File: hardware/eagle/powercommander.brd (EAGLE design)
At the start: 100 x 85 mm, 28 parts, among them IC1 ULN2803SO18-1, IC2 7805TV, IC3 MCP2551DIL8, K1 G5NB, K2 G5NB, K3 G5NB, K4 G5NB, K5 G5NB, K6 G5NB, K7 G5NB, K8 G5NB, X2 3KLEMME, X3 2KLEMME, X4 2KLEMME, X5 2KLEMME, X6 2KLEMME

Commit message: neu verkabelt
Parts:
- removed EXT2: EXT2, pinhead:2X13
- added D1, D2, D3, D4, D5, D6, D7, D8: (no value), diode:SOD323-W
- added D9: (no value), diode:MELF-MLL41
- added EXT2-1-4, EXT2-23-26: (no value), pinhead:2X02
- added F2: FUSESH35, fuse:SH25
- IC3: value MCP2551DIL8 -> MCP2551SOIC8; device personal-parts:DIL8 -> personal-parts:SOIC-08LG
- moved K1 16.3 mm to (57.1, 24.1)
- moved C3 11.4 mm to (58.4, 77.5)
- moved K3 5.24 mm to (41.9, 24.1)
- moved K7 5.24 mm to (11.4, 24.1)
- moved K8 5.24 mm to (3.81, 24.1)
- moved K2 5.24 mm to (49.5, 24.1)
- moved K4 5.24 mm to (34.3, 24.1)
- moved K5 5.24 mm to (26.7, 24.1)
- moved K6 5.24 mm to (19.1, 24.1)
- moved X5 5.08 mm to (24.2, 4.50)
- moved X6 5.08 mm to (14.1, 4.50)
- moved X3 5.08 mm to (44.6, 4.50)
- moved X4 5.08 mm to (34.4, 4.50)
- moved IC3 2.54 mm to (14.0, 59.7), flipped to the bottom, turned to 270 degrees
- moved C2 1.80 mm to (49.5, 76.2)
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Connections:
- net A2 renamed N$14
- net A4 renamed N$9
- net A6 renamed N$12
- net A8 renamed N$13
- removed net N$12 (its old number): IC1.14, K4.1
- removed net N$13 (its old number): IC1.15, K5.1
- removed net N$14 (its old number): IC1.16, K6.1
- removed net N$16: IC1.18, K8.1
- removed net N$21: EXT1.7, IC1.1
- removed net N$9 (its old number): IC1.11, K1.1
- new net N$22: F2.1, PHASE.2
- new net N$24: D8.A, IC1.18, K8.4
- new net N$26: D6.A, IC1.16, K6.4
- new net N$27: D5.A, IC1.15, K5.4
- new net N$28: D4.A, IC1.14, K4.4
- net +5V: now also D1.C, D2.C, D3.C, D4.C, D5.C, D6.C, D7.C, D8.C, D9.A, EXT2-23-26.4, K1.1, K2.1, K3.1, K4.1, K5.1, K6.1, K7.1, K8.1; no longer EXT2.26, K1.4, K2.4, K3.4, K4.4, K5.4, K6.4, K7.4, K8.4
- net N$10: now also D2.A, K2.4; no longer K2.1
- net N$11: now also D3.A, K3.4; no longer K3.1
- net N$15: now also D7.A, K7.4; no longer K7.1
- net N$2: now also X2.2; no longer X2.1
- net N$20: now also D1.A, IC1.11, K1.4; no longer EXT1.9, IC1.2
- net N$5: now also D9.C
- net N$6: now also X2.1; no longer X2.2
- net NULL: now also PHASE.1; no longer PHASE.2
- net PHASE: now also F2.2; no longer PHASE.1
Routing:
- net N$9 (its old number): track 49.9 -> 0.00 mm
- net N$16: track 32.3 -> 0.00 mm
- net N$24: track 0.00 -> 31.7 mm
- net N$20: track 9.13 -> 36.3 mm
- net N$35: track 25.7 -> 4.58 mm
- net N$14 (its old number): track 20.4 -> 0.00 mm
- net PHASE: track 134.3 -> 114.1 mm
- net N$12 (its old number): track 19.6 -> 0.00 mm
- net N$26: track 0.00 -> 19.1 mm
- net N$28: track 0.00 -> 17.5 mm
- net N$13 (its old number): track 17.0 -> 0.00 mm
- net N$27: track 0.00 -> 16.2 mm
- net N$22: track 0.00 -> 13.7 mm
- net N$21: track 10.5 -> 0.00 mm
- net N$19: track 8.60 -> 0.00 mm
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
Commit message: neue board version mit pwm pins
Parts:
- removed EXT2-23-26: (no value), pinhead:2X02
- added EXT2-21-26: (no value), pinhead:2X03
- moved JP3 34.4 mm to (6.30, 78.1), turned to 0 degrees
- moved IC3 32.3 mm to (46.2, 58.8), turned to 180 degrees
- moved R1 32.0 mm to (2.49, 70.5), turned to 270 degrees
- moved R2 28.8 mm to (5.03, 70.5), turned to 270 degrees
- moved R3 25.8 mm to (7.57, 70.5), turned to 270 degrees
- moved X2 9.00 mm to (21.6, 80.5)
- moved IC1 6.25 mm to (25.0, 53.8)
- flipped EXT1 to the bottom
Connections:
- removed net N$18 (its old number): EXT1.13, IC1.4
- removed net N$38: EXT1.16, R3.2
- removed net N$39: EXT1.14, R2.2
- removed net N$40: EXT1.12, R1.2
- new net N$16: EXT1.17, IC1.4
- new net N$21: EXT1.13, IC1.7
- new net N$25: EXT1.14, IC1.8
- new net N$29: EXT1.24, R1.2
- new net N$31: EXT1.18, R3.2
- net +5V: now also EXT2-21-26.6; no longer EXT2-23-26.4
- net N$1: now also EXT1.26, IC1.1; no longer EXT1.21, IC1.8
- net N$19: now also EXT1.16, IC1.6; no longer EXT1.11, IC1.3
- net N$30: now also EXT1.20, R2.2; no longer EXT1.26, IC1.10
- net N$7: now also EXT1.22, IC1.2; no longer EXT1.19, IC1.7
- net N$8: now also EXT1.21, IC1.3; no longer EXT1.17, IC1.6
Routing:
- net N$31: track 0.00 -> 25.8 mm
- net +5V: track 232.0 -> 209.4 mm
- net N$29: track 0.00 -> 21.2 mm
- net N$40: track 16.6 -> 0.00 mm
- net N$6: track 30.3 -> 45.0 mm
- net N$1: track 0.00 -> 12.1 mm
- net GND: track 12.1 -> 0.00 mm
- net N$39: track 11.9 -> 0.00 mm
- net N$7: track 0.00 -> 11.7 mm
- net N$2: track 28.8 -> 39.9 mm
- net N$25: track 0.00 -> 10.4 mm
- net N$19: track 0.00 -> 10.4 mm
- net N$8: track 0.00 -> 8.56 mm
- net N$30: track 32.0 -> 23.9 mm
- net N$38: track 7.77 -> 0.00 mm
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
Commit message: some fixes..
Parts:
- moved R3 8.10 mm to (13.9, 75.6), turned to 0 degrees
- moved R2 6.84 mm to (11.4, 73.1), turned to 0 degrees
- moved R1 6.27 mm to (8.76, 70.6), turned to 0 degrees
- moved X2 5.00 mm to (26.6, 80.5)
- moved JP3 3.05 mm to (8.78, 79.9)
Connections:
- net GND: now also EXT2-21-26.5
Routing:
- net N$29: track 21.2 -> 4.43 mm
- net N$30: track 23.9 -> 8.50 mm
- net N$31: track 25.8 -> 10.8 mm
- net N$32: track 3.81 -> 9.27 mm
- net N$36: track 3.81 -> 6.86 mm
- net N$6: track 45.0 -> 42.0 mm
- net N$2: track 39.9 -> 37.1 mm
- net N$37: track 3.81 -> 4.32 mm
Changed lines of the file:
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@@
 <element name="IC1" library="personal-parts" package="SO18-1" value="ULN2803SO18-1" x="25" y="53.75" rot="MR180"/>
 <element name="PHASE" library="personal-parts" package="W237-102" value="2KLEMME" x="91" y="4.5"/>
-<element name="X2" library="personal-parts" package="W237-103" value="3KLEMME" x="21.62" y="80.5" rot="R180"/>
+<element name="X2" library="personal-parts" package="W237-103" value="3KLEMME" x="26.62" y="80.5" rot="R180"/>
 <element name="IC2" library="linear" package="TO220V" value="7805TV" x="64.77" y="76.2" rot="R270"/>
 <element name="B1" library="rectifier" package="RB1A" value="rectifier" x="87.63" y="76.2"/>
@@
 <element name="X6" library="personal-parts" package="W237-102" value="2KLEMME" x="14.08" y="4.5"/>
 <element name="IC3" library="personal-parts" package="SOIC-08LG" value="MCP2551SOIC8" x="46.25" y="58.75" rot="MR180"/>
-<element name="JP3" library="pinhead" package="1X04" value="LEDS" x="6.3" y="78.14"/>
-<element name="R1" library="rcl" package="0204/7" value="280R" x="2.49" y="70.52" rot="R270"/>
-<element name="R2" library="rcl" package="0204/7" value="280R" x="5.03" y="70.52" rot="R270"/>
-<element name="R3" library="rcl" package="0204/7" value="280R" x="7.57" y="70.52" rot="R270"/>
+<element name="JP3" library="pinhead" package="1X04" value="LEDS" x="8.78" y="79.918"/>
+<element name="R1" library="rcl" package="0204/7" value="280R" x="8.758" y="70.645"/>
+<element name="R2" library="rcl" package="0204/7" value="280R" x="11.385" y="73.058"/>
+<element name="R3" library="rcl" package="0204/7" value="280R" x="13.885" y="75.598"/>
 <element name="F2" library="fuse" package="SH25" value="FUSESH35" x="85.09" y="16.51" rot="R180">
 <attribute name="OC_NEWARK" value="unknown" x="85.09" y="16.51" size="1.778" layer="27" rot="R180" display="off"/>
@@
 </polygon>
 <contactref element="EXT1" pad="6"/>
-<wire x1="38.735" y1="67.945" x2="45.615" y2="61.425" width="0" layer="19" extent="16-16"/>
+<contactref element="EXT2-21-26" pad="5"/>
 </signal>
 <signal name="A1">
@@
 <contactref element="JP3" pad="1"/>
 <contactref element="R1" pad="1"/>
-<wire x1="2.49" y1="78.14" x2="2.49" y2="74.33" width="1.27" layer="16"/>
+<wire x1="4.97" y1="79.918" x2="4.948" y2="70.645" width="1.27" layer="16"/>
 </signal>
 <signal name="N$36">
 <contactref element="JP3" pad="2"/>
 <contactref element="R2" pad="1"/>
-<wire x1="5.03" y1="78.14" x2="5.03" y2="74.33" width="1.27" layer="16"/>
+<wire x1="7.51" y1="79.918" x2="7.575" y2="73.058" width="1.27" layer="16"/>
 </signal>
 <signal name="N$37">
 <contactref element="JP3" pad="3"/>
 <contactref element="R3" pad="1"/>
-<wire x1="7.57" y1="78.14" x2="7.57" y2="74.33" width="1.27" layer="16"/>
+<wire x1="10.05" y1="79.918" x2="10.075" y2="75.598" width="1.27" layer="16"/>
 </signal>
 <signal name="N$11">
@@
 <wire x1="40" y1="53.75" x2="35" y2="58.75" width="0.4064" layer="16"/>
 <wire x1="35" y1="58.75" x2="35" y2="72.14" width="0.4064" layer="16"/>
-<wire x1="35" y1="72.14" x2="26.62" y2="80.52" width="0.4064" layer="16"/>
+<wire x1="35" y1="72.14" x2="31.62" y2="80.52" width="0.4064" layer="16"/>
 </signal>
 <signal name="N$6">
@@
 <wire x1="40" y1="52.5" x2="32.5" y2="60" width="0.4064" layer="16"/>
 <wire x1="32.5" y1="60" x2="32.5" y2="69.64" width="0.4064" layer="16"/>
-<wire x1="32.5" y1="69.64" x2="21.62" y2="80.52" width="0.4064" layer="16"/>
+<wire x1="32.5" y1="69.64" x2="26.62" y2="80.52" width="0.4064" layer="16"/>
 </signal>
 <signal name="N$29">
 <contactref element="EXT1" pad="24"/>
 <contactref element="R1" pad="2"/>
-<wire x1="15.875" y1="67.945" x2="15.875" y2="69.469" width="0.4064" layer="16"/>
-<wire x1="15.875" y1="69.469" x2="15.113" y2="70.231" width="0.4064" layer="16"/>
-<wire x1="15.113" y1="70.231" x2="10.668" y2="70.231" width="0.4064" layer="16"/>
-<wire x1="10.668" y1="70.231" x2="10.668" y2="66.421" width="0.4064" layer="16"/>
-<wire x1="10.668" y1="66.421" x2="8.255" y2="64.008" width="0.4064" layer="16"/>
-<wire x1="8.255" y1="64.008" x2="5.192" y2="64.008" width="0.4064" layer="16"/>
-<wire x1="5.192" y1="64.008" x2="2.49" y2="66.71" width="0.4064" layer="16"/>
+<wire x1="15.875" y1="67.945" x2="13.175" y2="70.645" width="1.27" layer="16" curve="90"/>
+<wire x1="13.175" y1="70.645" x2="12.568" y2="70.645" width="1.27" layer="16"/>
 </signal>
 <signal name="N$30">
 <contactref element="EXT1" pad="20"/>
 <contactref element="R2" pad="2"/>
-<wire x1="20.955" y1="67.945" x2="20.955" y2="69.088" width="0.4064" layer="16"/>
-<wire x1="20.955" y1="69.088" x2="18.542" y2="71.501" width="0.4064" layer="16"/>
-<wire x1="18.542" y1="71.501" x2="9.779" y2="71.501" width="0.4064" layer="16"/>
-<wire x1="9.779" y1="71.501" x2="9.652" y2="71.374" width="0.4064" layer="16"/>
-<wire x1="9.652" y1="71.374" x2="9.652" y2="67.056" width="0.4064" layer="16"/>
-<wire x1="9.652" y1="67.056" x2="7.747" y2="65.151" width="0.4064" layer="16"/>
-<wire x1="7.747" y1="65.151" x2="6.589" y2="65.151" width="0.4064" layer="16"/>
-<wire x1="6.589" y1="65.151" x2="5.03" y2="66.71" width="0.4064" layer="16"/>
+<wire x1="20.955" y1="67.945" x2="20.955" y2="69.85" width="1.27" layer="16"/>
+<wire x1="20.955" y1="69.85" x2="15.195" y2="73.058" width="1.27" layer="16"/>
 </signal>
 <signal name="N$31">
 <contactref element="EXT1" pad="18"/>
 <contactref element="R3" pad="2"/>
-<wire x1="7.57" y1="66.71" x2="7.57" y2="71.18" width="0.4064" layer="16"/>
-<wire x1="7.57" y1="71.18" x2="7.5" y2="72.52" width="0.4064" layer="16"/>
-<wire x1="7.5" y1="72.52" x2="22.5" y2="72.52" width="0.4064" layer="16"/>
-<wire x1="22.5" y1="72.52" x2="23.75" y2="70" width="0.4064" layer="16"/>
-<wire x1="23.75" y1="70" x2="23.75" y2="68.2" width="0.4064" layer="16"/>
-<wire x1="23.75" y1="68.2" x2="23.495" y2="67.945" width="0.4064" layer="16"/>
+<wire x1="23.495" y1="67.945" x2="23.495" y2="70.993" width="1.27" layer="16"/>
+<wire x1="23.495" y1="70.993" x2="18.89" y2="75.598" width="1.27" layer="16"/>
+<wire x1="18.89" y1="75.598" x2="17.695" y2="75.598" width="1.27" layer="16"/>
 </signal>
 </signals>

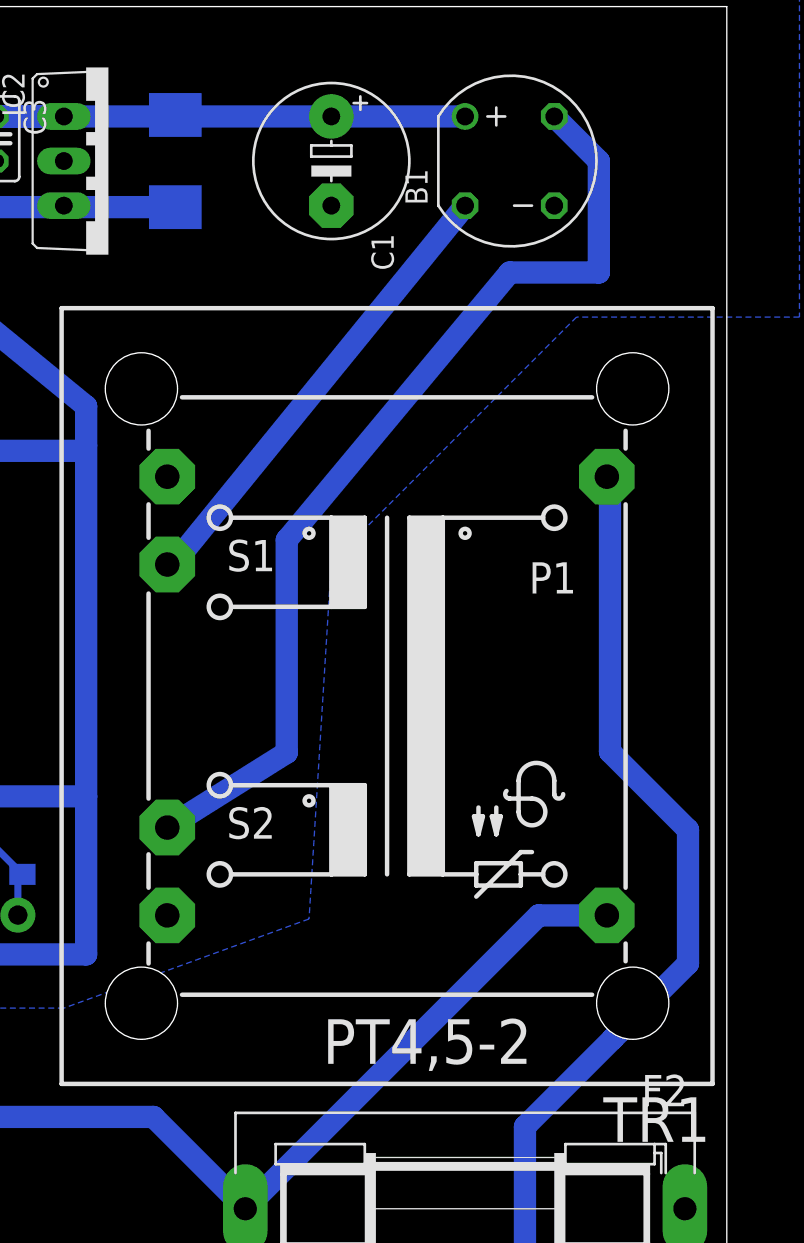
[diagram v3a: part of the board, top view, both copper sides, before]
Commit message: removed transformer holes
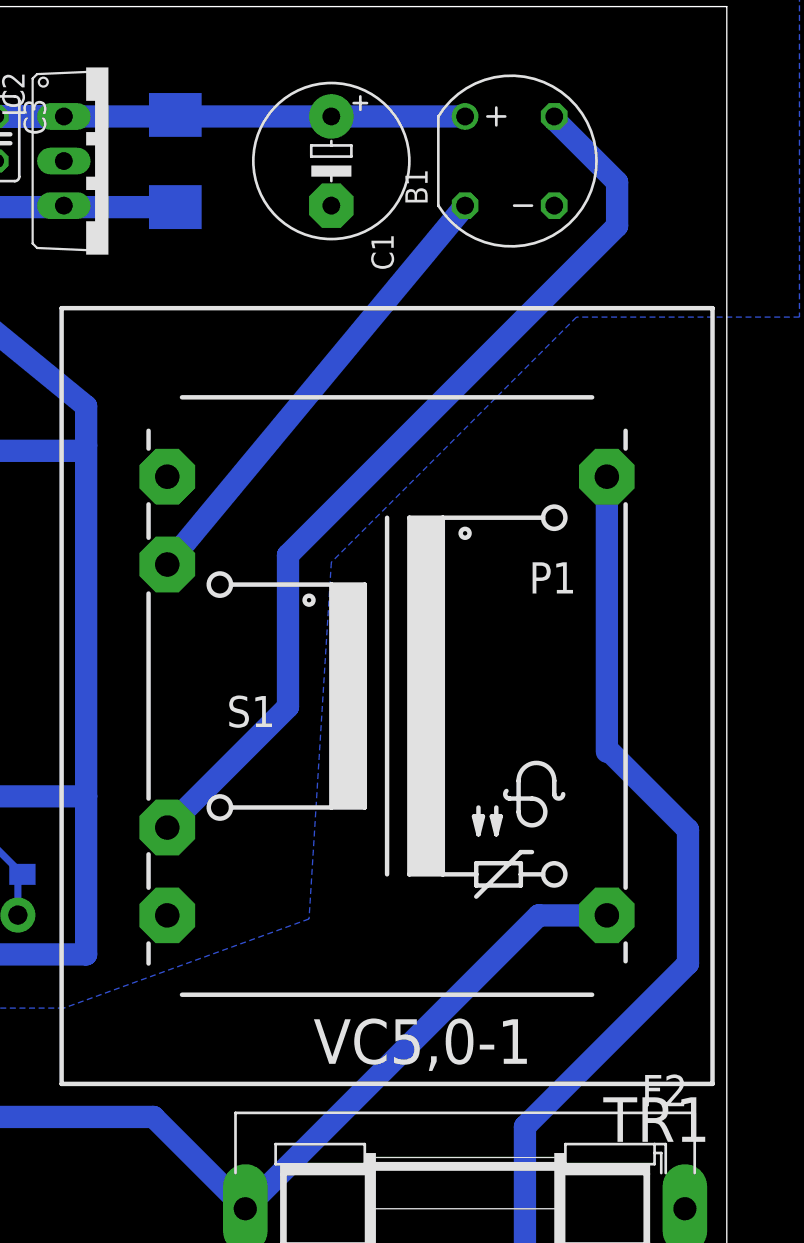
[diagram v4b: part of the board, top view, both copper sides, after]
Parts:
- TR1: value TRAFO 9V 556mA -> (none); device trafo:PT04,5-2 -> personal-parts:VC5,0-1
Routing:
- net N$4: track 55.0 -> 52.6 mm
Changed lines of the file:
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@@
 <element name="IC2" library="linear" package="TO220V" value="7805TV" x="64.77" y="76.2" rot="R270"/>
 <element name="B1" library="rectifier" package="RB1A" value="rectifier" x="87.63" y="76.2"/>
-<element name="TR1" library="trafo" package="PT04,5-2" value="TRAFO 9V 556mA" x="80.645" y="45.72" rot="R180"/>
 <element name="K1" library="relay-omron-G5NB" package="G5NB" value="G5NB" x="57.15" y="24.13" rot="R270">
 <attribute name="OC_NEWARK" value="unknown" x="-33.02" y="0" size="1.778" layer="27" rot="R270" display="off"/>
@@
 <element name="EXT2-21-26" library="pinhead" package="2X03" value="" x="41.075" y="41.275" rot="MR180"/>
 <element name="EXT2-1-4" library="pinhead" package="2X02" value="" x="14.605" y="41.275" rot="R270"/>
+<element name="TR1" library="personal-parts" package="VC5,0-1" value="" x="80.645" y="45.72" rot="R180"/>
 </elements>
 <signals>
 <signal name="PHASE">
-<contactref element="TR1" pad="1"/>
 <contactref element="K8" pad="2"/>
 <contactref element="K7" pad="2"/>
@@
 <wire x1="72.5678" y1="16.51" x2="67.3378" y2="21.74" width="1.27" layer="16"/>
 <wire x1="67.3378" y1="21.74" x2="54.91" y2="21.74" width="1.27" layer="16"/>
+<wire x1="89.281" y1="33.2232" x2="72.5678" y2="16.51" width="1.27" layer="16"/>
+<contactref element="TR1" pad="1"/>
 <wire x1="93.1672" y1="33.2232" x2="89.281" y2="33.2232" width="1.27" layer="16"/>
-<wire x1="89.281" y1="33.2232" x2="72.5678" y2="16.51" width="1.27" layer="16"/>
 </signal>
 <signal name="NULL">
-<contactref element="TR1" pad="2"/>
-<wire x1="93.5" y1="26.19" x2="93.98" y2="26.67" width="1.27" layer="16"/>
-<wire x1="93.98" y1="26.67" x2="97.79" y2="30.48" width="1.27" layer="16"/>
 <wire x1="97.79" y1="30.48" x2="97.79" y2="38.1" width="1.27" layer="16"/>
 <wire x1="97.79" y1="38.1" x2="93.345" y2="42.545" width="1.27" layer="16"/>
-<wire x1="93.345" y1="42.545" x2="93.345" y2="58.039" width="1.27" layer="16"/>
-<wire x1="93.345" y1="58.039" x2="93.1672" y2="58.2168" width="0.4064" layer="16"/>
 <contactref element="PHASE" pad="1"/>
 <wire x1="88.5" y1="4.5" x2="88.5" y2="21.19" width="1.27" layer="16"/>
-<wire x1="88.5" y1="21.19" x2="93.5" y2="26.19" width="1.27" layer="16"/>
-</signal>
-<signal name="N$3">
-<contactref element="TR1" pad="5"/>
-<contactref element="B1" pad="AC1"/>
-<wire x1="68.1228" y1="38.227" x2="74.93" y2="42.4942" width="1.27" layer="16"/>
-<wire x1="74.93" y1="42.4942" x2="74.93" y2="54.61" width="1.27" layer="16"/>
-<wire x1="74.93" y1="54.61" x2="87.63" y2="69.85" width="1.27" layer="16"/>
-<wire x1="87.63" y1="69.85" x2="92.71" y2="69.85" width="1.27" layer="16"/>
-<wire x1="92.71" y1="69.85" x2="92.71" y2="76.2" width="1.27" layer="16"/>
-<wire x1="92.71" y1="76.2" x2="90.17" y2="78.74" width="1.27" layer="16"/>
-</signal>
-<signal name="N$4">
-<contactref element="TR1" pad="4"/>
-<contactref element="B1" pad="AC2"/>
-<wire x1="68.1228" y1="53.213" x2="68.453" y2="53.213" width="0.4064" layer="16"/>
-<wire x1="68.453" y1="53.213" x2="85.09" y2="73.66" width="1.27" layer="16"/>
+<wire x1="88.5" y1="21.19" x2="97.79" y2="30.48" width="1.27" layer="16"/>
+<contactref element="TR1" pad="2"/>
+<wire x1="93.345" y1="42.545" x2="93.1672" y2="42.545" width="0.4064" layer="16"/>
+<wire x1="93.1672" y1="42.545" x2="93.1672" y2="58.2168" width="1.27" layer="16"/>
 </signal>
 <signal name="N$5">
@@
 <wire x1="18.89" y1="75.598" x2="17.695" y2="75.598" width="1.27" layer="16"/>
 </signal>
+<signal name="N$3">
+<contactref element="TR1" pad="4"/>
+<contactref element="B1" pad="AC2"/>
+<wire x1="68.1228" y1="53.213" x2="85.09" y2="73.66" width="1.27" layer="16"/>
+</signal>
+<signal name="N$4">
+<contactref element="TR1" pad="5"/>
+<contactref element="B1" pad="AC1"/>
+<wire x1="68.1228" y1="38.227" x2="75" y2="45.1042" width="1.27" layer="16"/>
+<wire x1="75" y1="45.1042" x2="75" y2="53.75" width="1.27" layer="16"/>
+<wire x1="75" y1="53.75" x2="93.75" y2="72.5" width="1.27" layer="16"/>
+<wire x1="93.75" y1="72.5" x2="93.75" y2="75" width="1.27" layer="16"/>
+<wire x1="93.75" y1="75" x2="90.17" y2="78.58" width="1.27" layer="16"/>
+<wire x1="90.17" y1="78.58" x2="90.17" y2="78.74" width="1.27" layer="16"/>
+</signal>
 </signals>

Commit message: board and schematic fancyfied
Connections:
- net N$1 renamed 1B
- net N$16 renamed 4B
- net N$17 renamed 5B
- net N$18 renamed CAN_RX
- net N$19 renamed 6B
- net N$21 renamed 7B
- net N$22 renamed L
- net N$23 renamed CAN_TX
- net N$25 renamed 8B
- net N$29 renamed LED1
- net N$30 renamed LED2
- net N$31 renamed LED3
- net N$7 renamed 2B
- net N$8 renamed 3B
- net PHASE renamed L_FUSE
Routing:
- net LED1: track 4.43 -> 5.39 mm
- net LED2: track 8.50 -> 9.10 mm
